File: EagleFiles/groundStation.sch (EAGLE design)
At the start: 5 parts

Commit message: small changes in motor control
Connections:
- removed net N$13: U$2.GND
- removed net N$14: U$2.FLT_N
- removed net N$26: U$4.FLT_N
- net GND: now also U$2.GND
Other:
- note added: "controller and wifi"
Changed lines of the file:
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@@
 <text x="302.26" y="78.74" size="1.778" layer="91">1</text>
 <text x="302.26" y="30.48" size="1.778" layer="91">2</text>
+<text x="2.54" y="22.86" size="1.778" layer="91">controller and wifi</text>
 </plain>
 <instances>
@@
 <segment>
 <pinref part="U$4" gate="G$1" pin="GND"/>
-<wire x1="325.12" y1="38.1" x2="337.82" y2="38.1" width="0.1524" layer="91"/>
+<wire x1="325.12" y1="38.1" x2="335.28" y2="38.1" width="0.1524" layer="91"/>
 <label x="335.28" y="38.1" size="1.778" layer="95" align="bottom-right"/>
 </segment>
@@
 <wire x1="0" y1="38.1" x2="-15.24" y2="38.1" width="0.1524" layer="91"/>
 <label x="-12.7" y="38.1" size="1.778" layer="95"/>
+</segment>
+<segment>
+<pinref part="U$2" gate="G$1" pin="GND"/>
+<wire x1="325.12" y1="86.36" x2="335.28" y2="86.36" width="0.1524" layer="91"/>
+<label x="335.28" y="86.36" size="1.778" layer="95" align="bottom-right"/>
 </segment>
 </net>
@@
 </segment>
 </net>
-<net name="N$13" class="0">
-<segment>
-<pinref part="U$2" gate="G$1" pin="GND"/>
-<wire x1="325.12" y1="86.36" x2="337.82" y2="86.36" width="0.1524" layer="91"/>
-<label x="335.28" y="86.36" size="1.778" layer="95" align="bottom-right"/>
-</segment>
-</net>
-<net name="N$14" class="0">
-<segment>
-<pinref part="U$2" gate="G$1" pin="FLT_N"/>
-<wire x1="325.12" y1="88.9" x2="337.82" y2="88.9" width="0.1524" layer="91"/>
-<label x="335.28" y="88.9" size="1.778" layer="95" align="bottom-right"/>
-</segment>
-</net>
 <net name="V_EXTERNAL" class="0">
 <segment>
@@
 </segment>
 </net>
-<net name="N$26" class="0">
-<segment>
-<pinref part="U$4" gate="G$1" pin="FLT_N"/>
-<wire x1="325.12" y1="40.64" x2="337.82" y2="40.64" width="0.1524" layer="91"/>
-<label x="335.28" y="40.64" size="1.778" layer="95" align="bottom-right"/>
-</segment>
-</net>

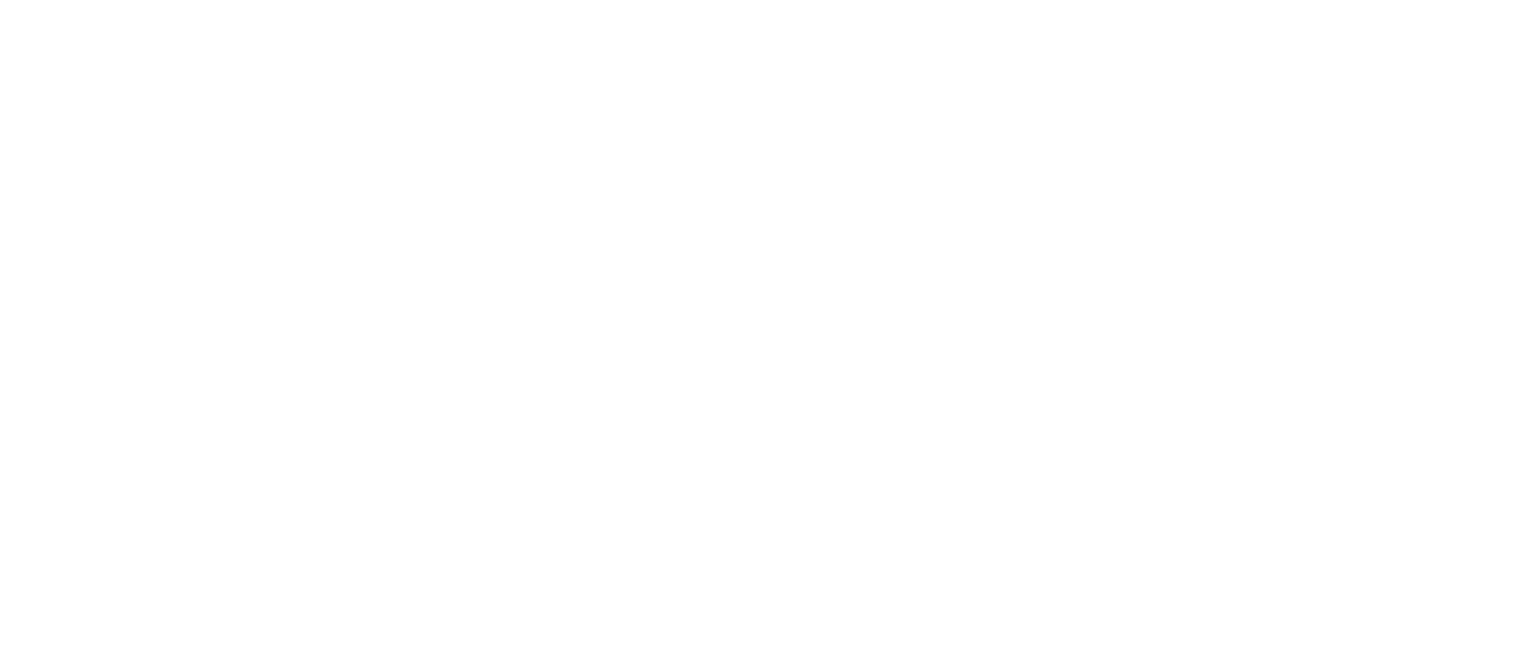
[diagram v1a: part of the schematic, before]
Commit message: added basic circuit for rffm tp4056
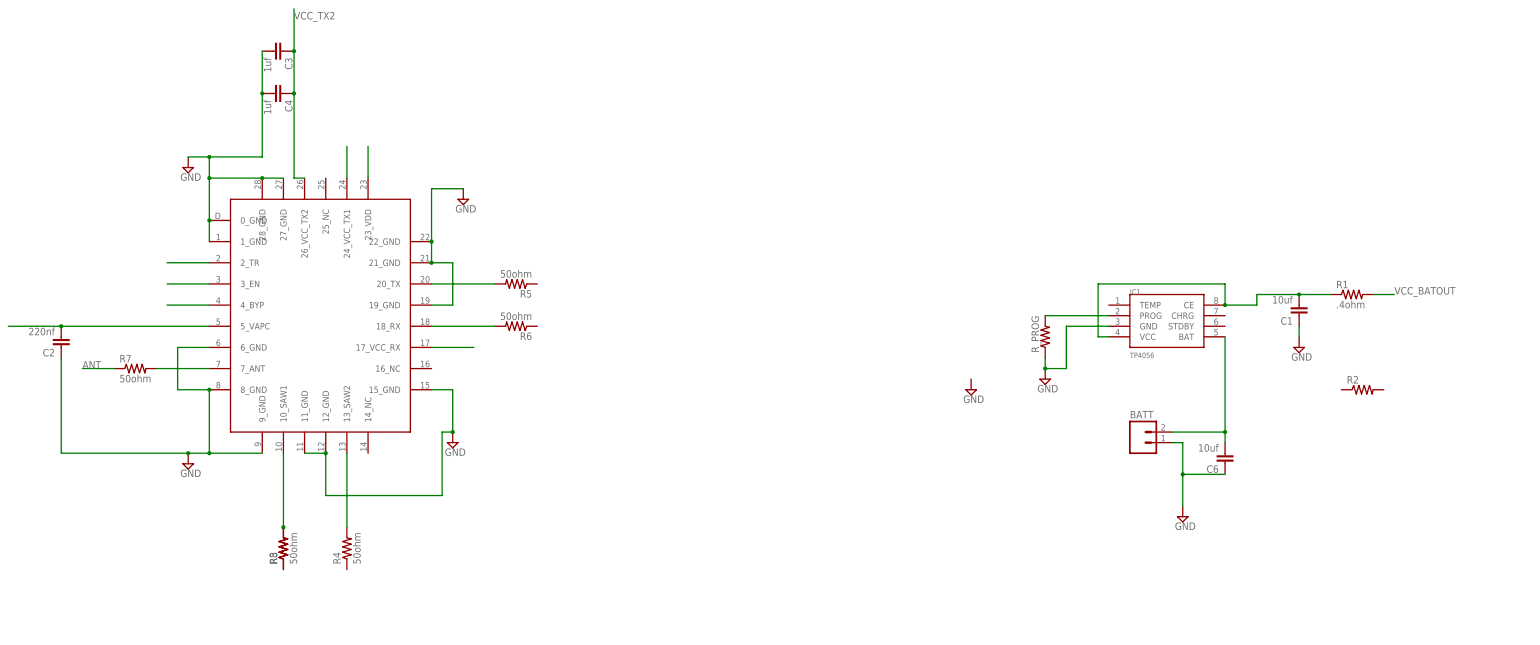
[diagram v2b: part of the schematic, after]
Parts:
- added BATT: (no value), con-amp-quick:M02
- added C1, C6: 10uf, SparkFun-Capacitors:0.1UF-0603-100V-10%
- added C2: 220nf, SparkFun-Capacitors:0.1UF-0603-100V-10%
- added C3, C4: 1uf, SparkFun-Capacitors:0.1UF-0603-100V-10%
- added IC1: TP4056, TP4056:TP4056
- added R1: .4ohm, adafruit:R-US_R0603
- added R2, R3, R_PROG: (no value), adafruit:R-US_R0603
- added R4, R5, R6, R7, R8: 50ohm, adafruit:R-US_R0603
- added U$3: RFFM6404, RFFM6406:RFFM6404
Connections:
- new net ANT: R7.1
- new net N$1: BATT.2, C6.2, IC1.BAT
- new net N$12: R4.2, U$3.13_SAW2
- new net N$13: R5.2, U$3.20_TX
- new net N$14: R6.2, U$3.18_RX
- new net N$15: U$3.17_VCC_RX
- new net N$17: U$3.23_VDD
- new net N$18: U$3.24_VCC_TX1
- new net N$19: U$3.2_TR
- new net N$2: C1.2, IC1.CE, IC1.VCC, R1.1
- new net N$20: U$3.3_EN
- new net N$21: U$3.4_BYP
- new net N$3: IC1.PROG, R_PROG.2
- new net N$4: R3.2, R8.2, U$3.10_SAW1
- new net N$6: R3.1, R8.1
- new net N$7: R7.2, U$3.7_ANT
- new net N$9: C2.2, U$3.5_VAPC
- new net VCC_BATOUT: R1.2
- new net VCC_TX2: C3.1, C4.1, U$3.26_VCC_TX2
- net GND: now also BATT.1, C1.1, C2.1, C3.2, C4.2, C6.1, IC1.GND, R_PROG.1, U$3.0_GND, U$3.11_GND, U$3.12_GND, U$3.15_GND, U$3.19_GND, U$3.1_GND, U$3.21_GND, U$3.22_GND, U$3.27_GND, U$3.28_GND, U$3.6_GND, U$3.8_GND, U$3.9_GND

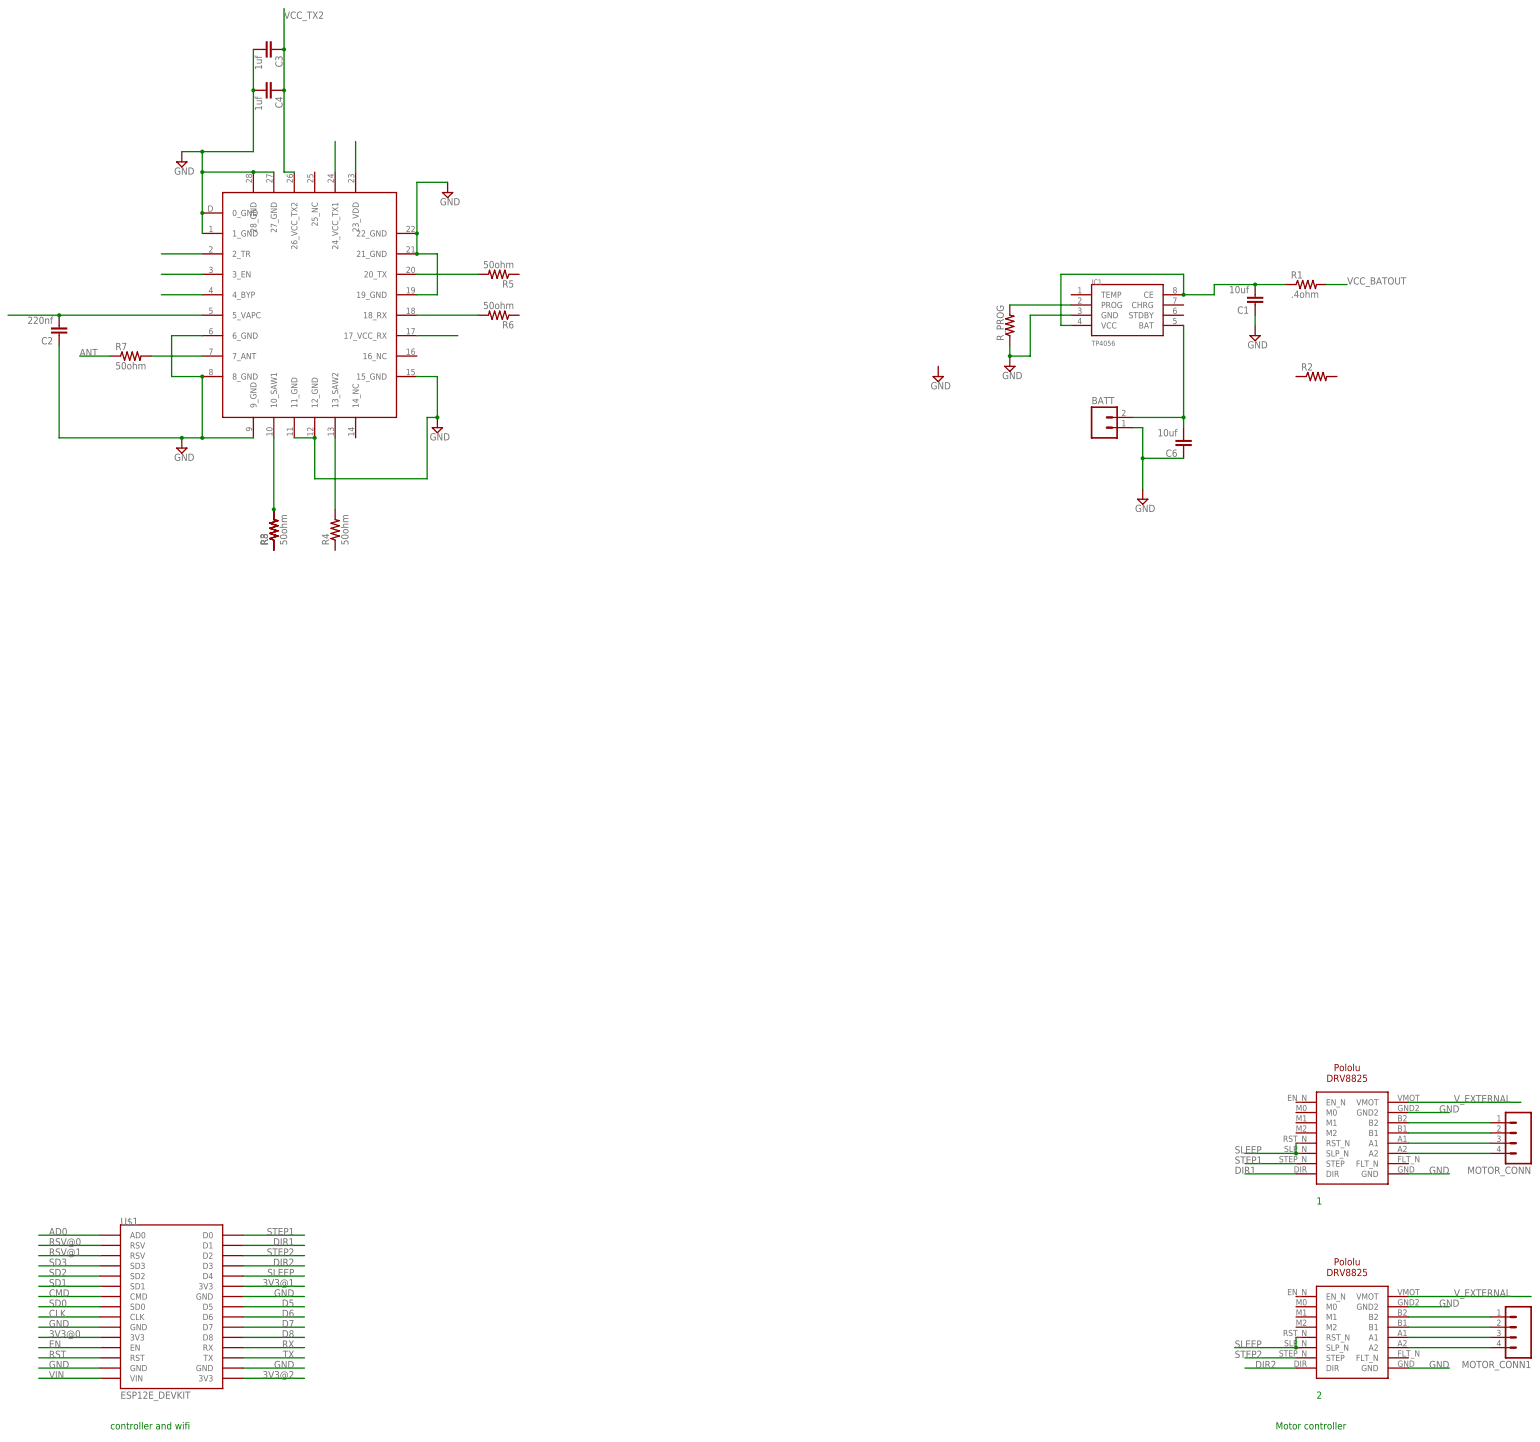
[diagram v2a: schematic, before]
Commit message: added the basic battery circuit
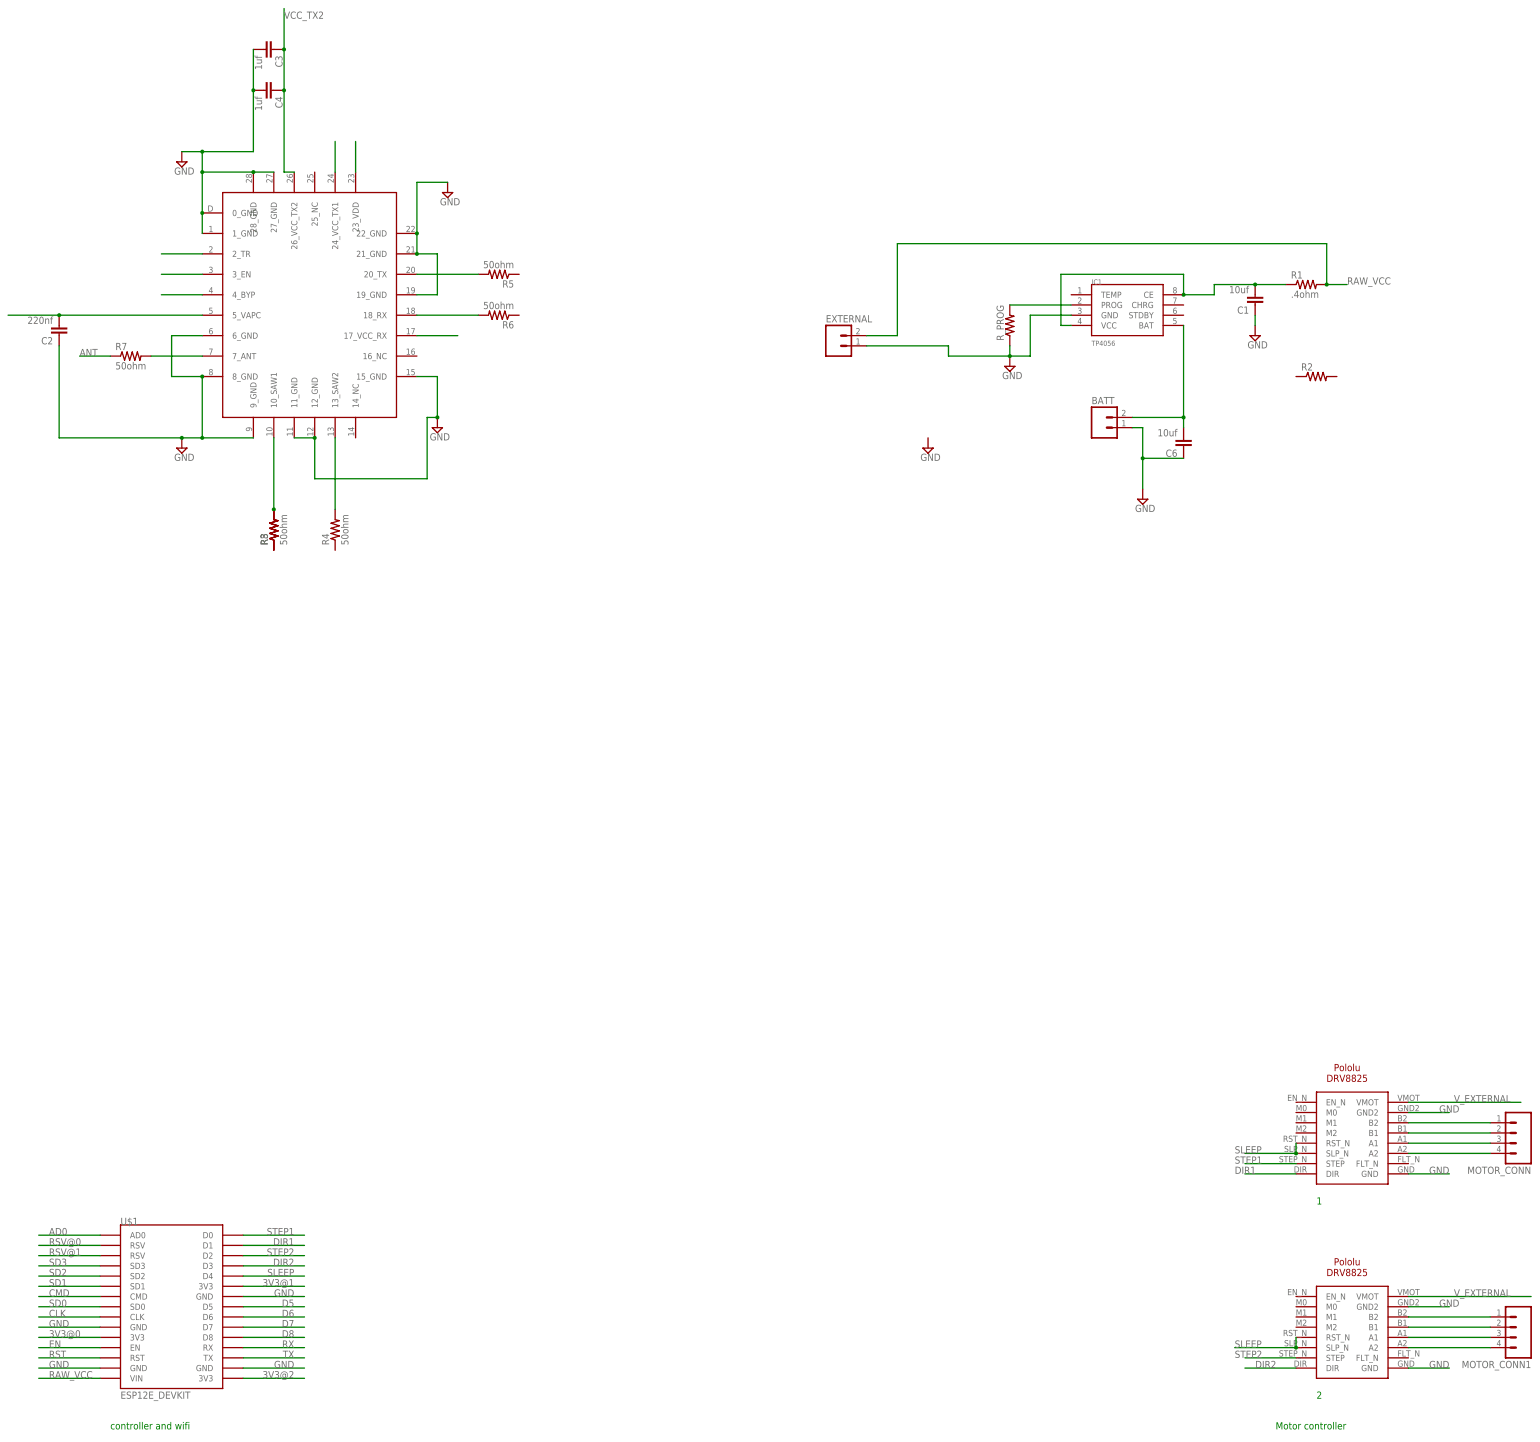
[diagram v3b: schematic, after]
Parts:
- added EXTERNAL: (no value), con-amp-quick:M02
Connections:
- removed net VCC_BATOUT: R1.2
- removed net VIN: U$1.VIN
- new net RAW_VCC: EXTERNAL.2, R1.2, U$1.VIN
- net GND: now also EXTERNAL.1
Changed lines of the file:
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@@
 <part name="C4" library="SparkFun-Capacitors" deviceset="0.1UF" device="-0603-100V-10%" value="1uf"/>
 <part name="R8" library="adafruit" library_urn="urn:adsk.eagle:library:420" deviceset="R-US_" device="R0603" package3d_urn="urn:adsk.eagle:package:6240565/1" value="50ohm"/>
+<part name="EXTERNAL" library="con-amp-quick" library_urn="urn:adsk.eagle:library:125" deviceset="M02" device="" package3d_urn="urn:adsk.eagle:package:5956/1"/>
 </parts>
 <sheets>
@@
 <attribute name="VALUE" x="267.716" y="271.399" size="1.778" layer="96" font="vector" rot="R180"/>
 </instance>
-<instance part="SUPPLY3" gate="GND" x="208.28" y="284.48" smashed="yes">
-<attribute name="VALUE" x="206.375" y="281.305" size="1.778" layer="96"/>
+<instance part="SUPPLY3" gate="GND" x="205.74" y="266.7" smashed="yes">
+<attribute name="VALUE" x="203.835" y="263.525" size="1.778" layer="96"/>
 </instance>
 <instance part="SUPPLY4" gate="GND" x="226.06" y="287.02" smashed="yes">
@@
 <attribute name="NAME" x="41.6814" y="242.57" size="1.778" layer="95" rot="R90"/>
 <attribute name="VALUE" x="46.482" y="242.57" size="1.778" layer="96" rot="R90"/>
+</instance>
+<instance part="EXTERNAL" gate="G$1" x="182.88" y="292.1" smashed="yes">
+<attribute name="VALUE" x="180.34" y="287.02" size="1.778" layer="96"/>
+<attribute name="NAME" x="180.34" y="297.942" size="1.778" layer="95"/>
 </instance>
 </instances>
@@
 <wire x1="231.14" y1="289.56" x2="226.06" y2="289.56" width="0.1524" layer="91"/>
 <junction x="226.06" y="289.56"/>
+<pinref part="EXTERNAL" gate="G$1" pin="1"/>
+<wire x1="190.5" y1="292.1" x2="210.82" y2="292.1" width="0.1524" layer="91"/>
+<wire x1="210.82" y1="292.1" x2="210.82" y2="289.56" width="0.1524" layer="91"/>
+<wire x1="210.82" y1="289.56" x2="226.06" y2="289.56" width="0.1524" layer="91"/>
 </segment>
 <segment>
@@
 </segment>
 </net>
-<net name="VIN" class="0">
-<segment>
-<pinref part="U$1" gate="G$1" pin="VIN"/>
-<wire x1="0" y1="35.56" x2="-15.24" y2="35.56" width="0.1524" layer="91"/>
-<label x="-12.7" y="35.56" size="1.778" layer="95"/>
-</segment>
-</net>
 <net name="STEP2" class="0">
 <segment>
@@
 </segment>
 </net>
-<net name="VCC_BATOUT" class="0">
+<net name="RAW_VCC" class="0">
 <segment>
 <pinref part="R1" gate="G$1" pin="2"/>
 <wire x1="304.8" y1="307.34" x2="309.88" y2="307.34" width="0.1524" layer="91"/>
 <label x="309.88" y="307.34" size="1.778" layer="95"/>
-</segment>
-</net>
+<pinref part="EXTERNAL" gate="G$1" pin="2"/>
+<wire x1="190.5" y1="294.64" x2="198.12" y2="294.64" width="0.1524" layer="91"/>
+<wire x1="198.12" y1="294.64" x2="198.12" y2="317.5" width="0.1524" layer="91"/>
+<wire x1="198.12" y1="317.5" x2="304.8" y2="317.5" width="0.1524" layer="91"/>
+<wire x1="304.8" y1="317.5" x2="304.8" y2="307.34" width="0.1524" layer="91"/>
+<junction x="304.8" y="307.34"/>
+</segment>
+<segment>
+<pinref part="U$1" gate="G$1" pin="VIN"/>
+<wire x1="0" y1="35.56" x2="-15.24" y2="35.56" width="0.1524" layer="91"/>
+<label x="-12.7" y="35.56" size="1.778" layer="95"/>
+</segment>
+</net>
